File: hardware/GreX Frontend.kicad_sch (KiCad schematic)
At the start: 1 part, among them U28 DSA_Logo

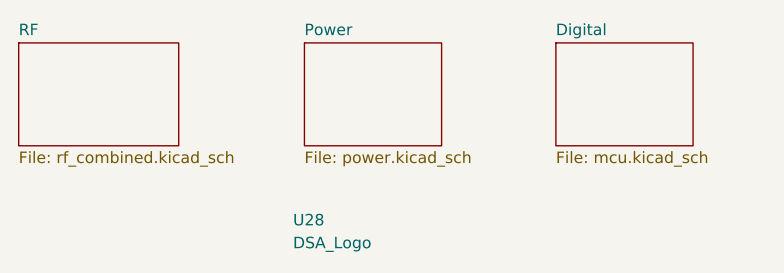
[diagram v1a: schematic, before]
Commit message: Update FEM hardware design for production version
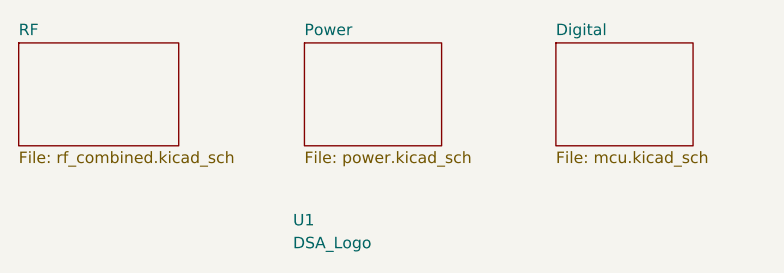
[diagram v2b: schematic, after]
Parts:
- renumbered U28 to U1
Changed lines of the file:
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@@
   (symbol (lib_id "DSA2000:DSA_Logo") (at 134.62 111.125 0) (unit 1)
     (in_bom yes) (on_board yes) (dnp no) (fields_autoplaced)
-    (property "Reference" "U28" (at 135.89 109.8549 0)
+    (property "Reference" "U1" (at 135.89 109.8549 0)
       (effects (font (size 1.27 1.27)) (justify left))
     )
@@
       (project "GreX Frontend"
         (path "/e63e39d7-6ac0-4ffd-8aa3-1841a4541b55"
-          (reference "U28") (unit 1)
+          (reference "U1") (unit 1)
         )
       )
